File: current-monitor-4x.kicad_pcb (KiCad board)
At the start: 2 copper layers, 35 x 30 mm, 32 parts, among them J1 CONN-2, J2 CONN-2, J3 USB-MICROB, J4 JTAG, U1 ACS711EX, U2 ACS711EX, U3 MKL26ZxxVFM4, Y1 12MHz

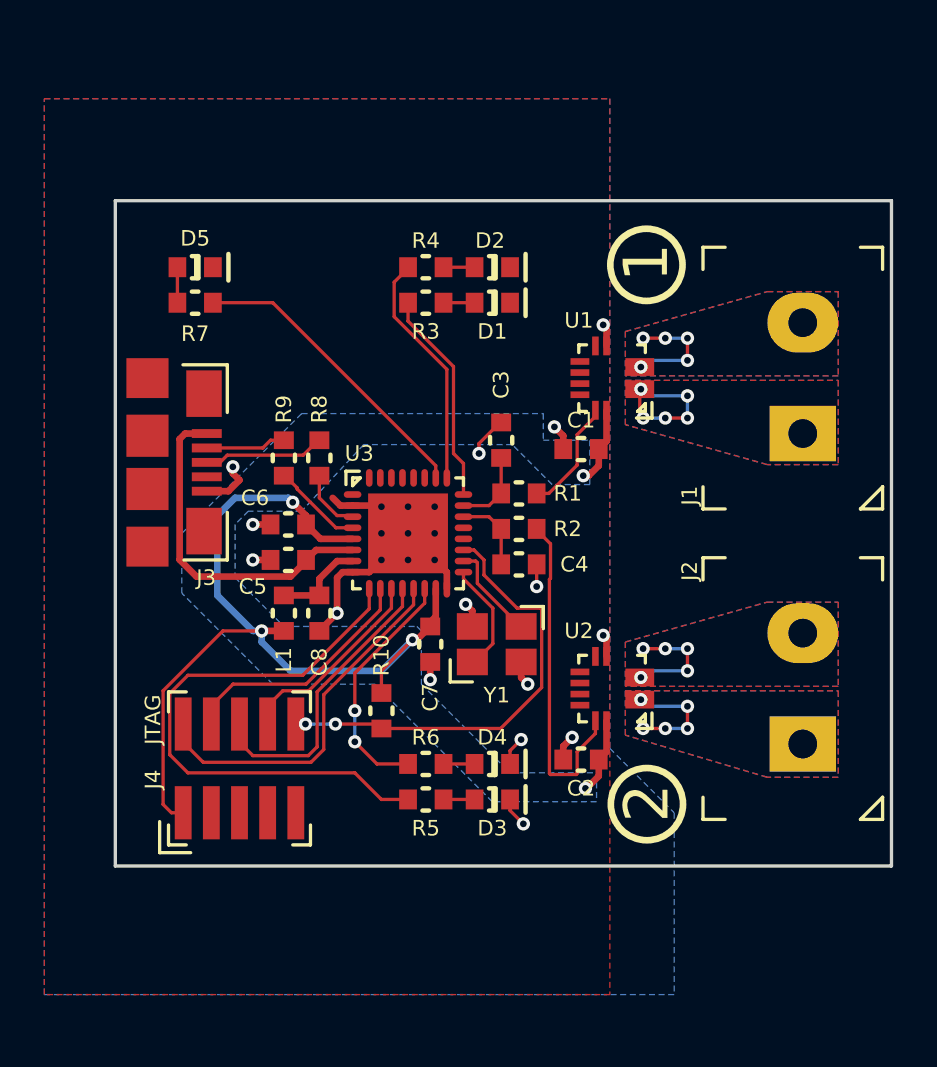
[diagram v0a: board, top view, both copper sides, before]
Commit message: add mounting lugs
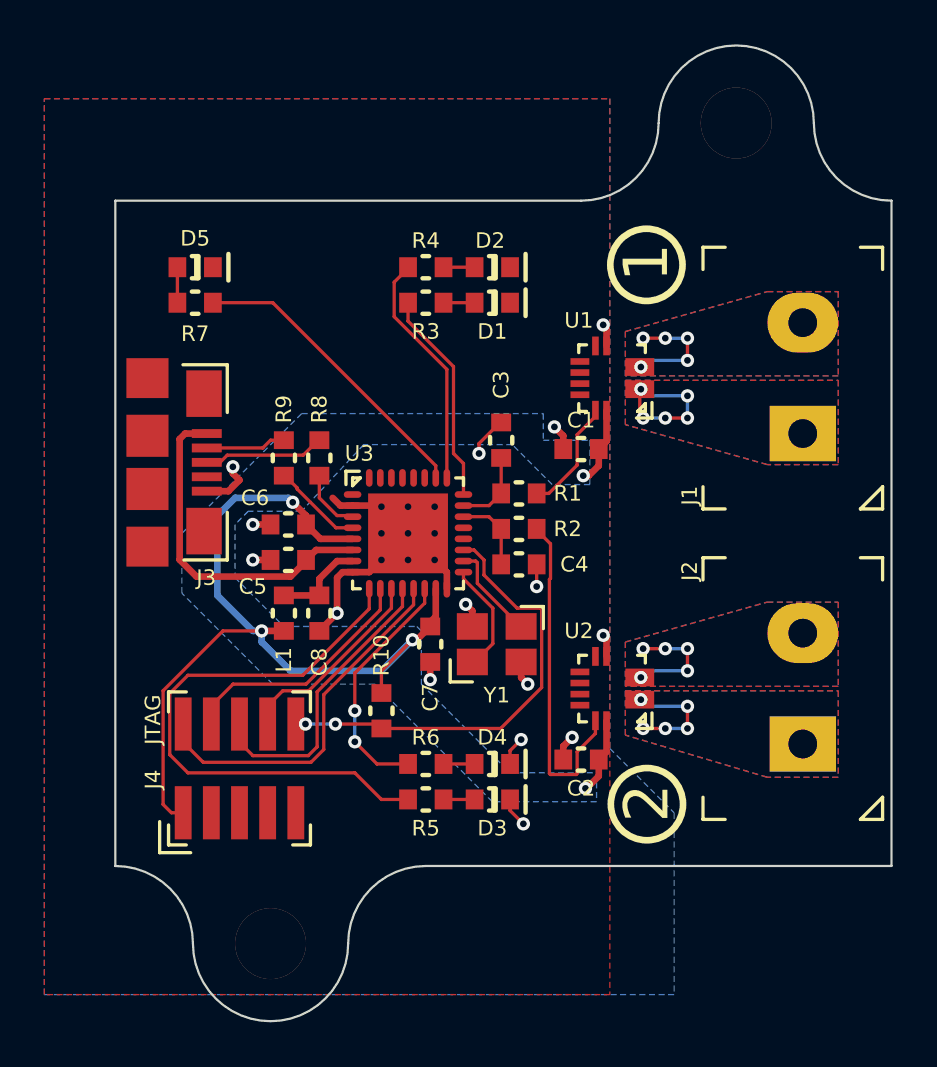
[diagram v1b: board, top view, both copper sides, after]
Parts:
- added REF**: M3-LUG, libs:M3-LUG, F.Cu at (170.0, 116.5)
- added REF**: M3-LUG, libs:M3-LUG, F.Cu at (191.0, 79.5)
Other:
- board size 35 x 30 mm -> 35 x 44 mm
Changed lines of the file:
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@@
     (links 97)
     (no_connects 0)
-    (area 162.924999 82.924999 198.075001 113.075001)
+    (area 162.949999 75.949999 198.050001 120.050001)
     (thickness 1.6)
-    (drawings 8)
+    (drawings 14)
     (tracks 282)
     (zones 0)
-    (modules 32)
+    (modules 34)
     (nets 34)
   )
   (page A4)
+  (title_block
+    (title "2x Isolated Current Monitor")
+    (date 2015-11-08)
+    (rev 1.0)
+    (company sternlabs)
+    (comment 1 "(c) 2015 Simon Schubert")
+  )
   (layers
     (0 F.Cu signal)
@@
     (trace_min 0.15)
     (segment_width 0.2)
-    (edge_width 0.15)
+    (edge_width 0.1)
     (via_size 0.6)
     (via_drill 0.3)
@@
     (add_net "Net-(U3-Pad17)")
     (add_net "Net-(U3-Pad18)")
+  )
+  (module libs:M3-LUG (layer F.Cu)
+    (at 170 116.5 180)
+    (fp_text reference REF** (at 0 0.5 180) (layer F.SilkS) hide
+      (effects (font (size 1 1) (thickness 0.15)))
+    )
+    (fp_text value M3-LUG (at 0 -0.5 180) (layer F.Fab) hide
+      (effects (font (size 1 1) (thickness 0.15)))
+    )
+    (fp_arc (start -7 0) (end -3.5 0) (angle 90) (layer Dwgs.User) (width 0.1))
+    (fp_arc (start 7 0) (end 3.5 0) (angle -90) (layer Dwgs.User) (width 0.1))
+    (fp_arc (start 0 0) (end -3.5 0) (angle 180) (layer Dwgs.User) (width 0.1))
+    (pad 1 thru_hole circle (at 0 0 180) (size 3.2 3.2) (drill 3.2) (layers *.Cu *.Mask))
   )
   (module libs:CONN-2x5-1.27-SMT (layer F.Cu)
@@
       (net 15 "Net-(J1-Pad2)") (thermal_width 0.5) (thermal_gap 0.3))
   )
+  (module libs:M3-LUG (layer F.Cu)
+    (at 191 79.5)
+    (fp_text reference REF** (at 0 0.5) (layer F.SilkS) hide
+      (effects (font (size 1 1) (thickness 0.15)))
+    )
+    (fp_text value M3-LUG (at 0 -0.5) (layer F.Fab) hide
+      (effects (font (size 1 1) (thickness 0.15)))
+    )
+    (fp_arc (start -7 0) (end -3.5 0) (angle 90) (layer Dwgs.User) (width 0.1))
+    (fp_arc (start 7 0) (end 3.5 0) (angle -90) (layer Dwgs.User) (width 0.1))
+    (fp_arc (start 0 0) (end -3.5 0) (angle 180) (layer Dwgs.User) (width 0.1))
+    (pad 1 thru_hole circle (at 0 0) (size 3.2 3.2) (drill 3.2) (layers *.Cu *.Mask))
+  )
+  (gr_arc (start 170 116.5) (end 173.5 116.5) (angle 180) (layer Edge.Cuts) (width 0.1))
+  (gr_arc (start 177 116.5) (end 173.5 116.5) (angle 90) (layer Edge.Cuts) (width 0.1))
+  (gr_arc (start 163 116.5) (end 163 113) (angle 90) (layer Edge.Cuts) (width 0.1))
+  (gr_line (start 198 113) (end 177 113) (layer Edge.Cuts) (width 0.1))
+  (gr_arc (start 191 79.5) (end 187.5 79.5) (angle 180) (layer Edge.Cuts) (width 0.1))
+  (gr_arc (start 198 79.5) (end 198 83) (angle 90) (layer Edge.Cuts) (width 0.1))
+  (gr_arc (start 184 79.5) (end 187.5 79.5) (angle 90) (layer Edge.Cuts) (width 0.1))
   (gr_text 2 (at 186.972507 110.162173 90) (layer F.SilkS)
     (effects (font (size 2 2) (thickness 0.3)))
@@
     (effects (font (size 2 2) (thickness 0.3)))
   )
-  (gr_line (start 163 83) (end 198 83) (layer Edge.Cuts) (width 0.15))
-  (gr_line (start 163 113) (end 163 83) (layer Edge.Cuts) (width 0.15))
-  (gr_line (start 198 113) (end 163 113) (layer Edge.Cuts) (width 0.15))
-  (gr_line (start 198 83) (end 198 113) (layer Edge.Cuts) (width 0.15))
+  (gr_line (start 163 83) (end 184 83) (layer Edge.Cuts) (width 0.1))
+  (gr_line (start 163 113) (end 163 83) (layer Edge.Cuts) (width 0.1))
+  (gr_line (start 198 83) (end 198 113) (layer Edge.Cuts) (width 0.1))
   (segment (start 184.35 95.4) (end 184.1 95.4) (width 0.3) (layer F.Cu) (net 1))
   (segment (start 184.8 94.95) (end 184.35 95.4) (width 0.3) (layer F.Cu) (net 1))

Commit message: fix zone layout
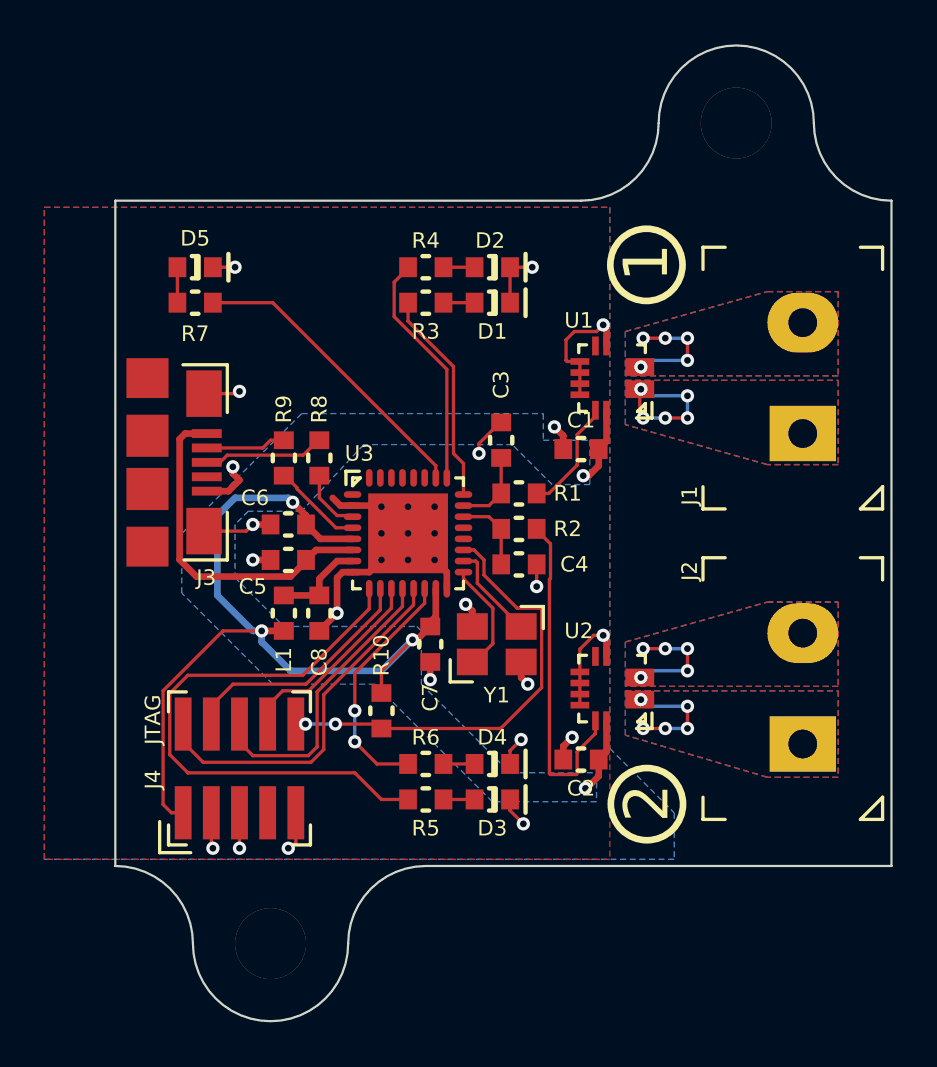
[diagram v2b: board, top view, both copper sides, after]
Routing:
- net COM: track 25.9 -> 47.3 mm, vias 15 -> 21
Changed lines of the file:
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@@
     (thickness 1.6)
     (drawings 14)
-    (tracks 282)
+    (tracks 317)
     (zones 0)
     (modules 34)
@@
   (title_block
     (title "2x Isolated Current Monitor")
-    (date 2015-11-08)
+    (date 2015-11-09)
     (rev 1.0)
     (company sternlabs)
@@
     (add_net "Net-(U3-Pad17)")
     (add_net "Net-(U3-Pad18)")
-  )
-  (module libs:M3-LUG (layer F.Cu)
-    (at 170 116.5 180)
-    (fp_text reference REF** (at 0 0.5 180) (layer F.SilkS) hide
-      (effects (font (size 1 1) (thickness 0.15)))
-    )
-    (fp_text value M3-LUG (at 0 -0.5 180) (layer F.Fab) hide
-      (effects (font (size 1 1) (thickness 0.15)))
-    )
-    (fp_arc (start -7 0) (end -3.5 0) (angle 90) (layer Dwgs.User) (width 0.1))
-    (fp_arc (start 7 0) (end 3.5 0) (angle -90) (layer Dwgs.User) (width 0.1))
-    (fp_arc (start 0 0) (end -3.5 0) (angle 180) (layer Dwgs.User) (width 0.1))
-    (pad 1 thru_hole circle (at 0 0 180) (size 3.2 3.2) (drill 3.2) (layers *.Cu *.Mask))
   )
   (module libs:CONN-2x5-1.27-SMT (layer F.Cu)
@@
       (effects (font (size 1 1) (thickness 0.15)))
     )
+    (fp_line (start 7 3.5) (end -7 3.5) (layer Margin) (width 0.1))
     (fp_arc (start -7 0) (end -3.5 0) (angle 90) (layer Dwgs.User) (width 0.1))
     (fp_arc (start 7 0) (end 3.5 0) (angle -90) (layer Dwgs.User) (width 0.1))
     (fp_arc (start 0 0) (end -3.5 0) (angle 180) (layer Dwgs.User) (width 0.1))
     (pad 1 thru_hole circle (at 0 0) (size 3.2 3.2) (drill 3.2) (layers *.Cu *.Mask))
+  )
+  (module libs:M3-LUG (layer F.Cu)
+    (at 170 116.5 180)
+    (fp_text reference REF** (at 0 0.5 180) (layer F.SilkS) hide
+      (effects (font (size 1 1) (thickness 0.15)))
+    )
+    (fp_text value M3-LUG (at 0 -0.5 180) (layer F.Fab) hide
+      (effects (font (size 1 1) (thickness 0.15)))
+    )
+    (fp_line (start 7 3.5) (end -7 3.5) (layer Margin) (width 0.1))
+    (fp_arc (start -7 0) (end -3.5 0) (angle 90) (layer Dwgs.User) (width 0.1))
+    (fp_arc (start 7 0) (end 3.5 0) (angle -90) (layer Dwgs.User) (width 0.1))
+    (fp_arc (start 0 0) (end -3.5 0) (angle 180) (layer Dwgs.User) (width 0.1))
+    (pad 1 thru_hole circle (at 0 0 180) (size 3.2 3.2) (drill 3.2) (layers *.Cu *.Mask))
   )
   (gr_arc (start 170 116.5) (end 173.5 116.5) (angle 180) (layer Edge.Cuts) (width 0.1))
@@
   (segment (start 173.7 98.25) (end 172.25 98.25) (width 0.3) (layer F.Cu) (net 1) (status 10))
   (segment (start 172.25 98.25) (end 171.6 97.6) (width 0.3) (layer F.Cu) (net 1) (status 20))
+  (segment (start 183.95 104.25) (end 183.95 103.225744) (width 0.15) (layer F.Cu) (net 2))
+  (segment (start 183.95 103.225744) (end 184.575736 102.600008) (width 0.15) (layer F.Cu) (net 2))
+  (segment (start 184.575736 102.600008) (end 185 102.600008) (width 0.15) (layer F.Cu) (net 2))
+  (segment (start 183.95 104.75) (end 183.95 104.25) (width 0.15) (layer F.Cu) (net 2))
+  (segment (start 183.95 105.25) (end 183.95 104.75) (width 0.15) (layer F.Cu) (net 2))
+  (segment (start 183.95 105.75) (end 183.95 105.25) (width 0.15) (layer F.Cu) (net 2))
+  (segment (start 167.4 86) (end 168.4 86) (width 0.15) (layer F.Cu) (net 2))
+  (via (at 168.4 86) (size 0.6) (drill 0.3) (layers F.Cu B.Cu) (net 2))
+  (segment (start 167 91.7) (end 168.5 91.7) (width 0.15) (layer F.Cu) (net 2))
+  (segment (start 168.5 91.7) (end 168.6 91.6) (width 0.15) (layer F.Cu) (net 2))
+  (via (at 168.6 91.6) (size 0.6) (drill 0.3) (layers F.Cu B.Cu) (net 2))
+  (segment (start 167 97.9) (end 168.900001 97.899999) (width 0.15) (layer F.Cu) (net 2))
+  (segment (start 168.900001 97.899999) (end 169.2 97.6) (width 0.15) (layer F.Cu) (net 2))
+  (segment (start 171.14 110.6) (end 171.14 111.95) (width 0.15) (layer F.Cu) (net 2))
+  (segment (start 171.14 111.95) (end 170.89 112.2) (width 0.15) (layer F.Cu) (net 2))
+  (segment (start 170.89 112.2) (end 170.8 112.2) (width 0.15) (layer F.Cu) (net 2))
+  (via (at 170.8 112.2) (size 0.6) (drill 0.3) (layers F.Cu B.Cu) (net 2))
+  (segment (start 168.6 110.6) (end 168.6 111.95) (width 0.15) (layer F.Cu) (net 2))
+  (segment (start 168.6 111.95) (end 168.6 112.2) (width 0.15) (layer F.Cu) (net 2))
+  (via (at 168.6 112.2) (size 0.6) (drill 0.3) (layers F.Cu B.Cu) (net 2))
+  (segment (start 167.33 110.6) (end 167.33 112.13) (width 0.15) (layer F.Cu) (net 2))
+  (segment (start 167.33 112.13) (end 167.4 112.2) (width 0.15) (layer F.Cu) (net 2))
+  (via (at 167.4 112.2) (size 0.6) (drill 0.3) (layers F.Cu B.Cu) (net 2))
+  (segment (start 183.325 89.275) (end 183.700001 88.899999) (width 0.15) (layer F.Cu) (net 2))
+  (segment (start 183.700001 88.899999) (end 184.700011 88.899999) (width 0.15) (layer F.Cu) (net 2))
+  (segment (start 184.700011 88.899999) (end 185.00001 88.6) (width 0.15) (layer F.Cu) (net 2))
+  (segment (start 183.325 90.2) (end 183.325 89.275) (width 0.15) (layer F.Cu) (net 2))
+  (segment (start 183.95 90.25) (end 183.375 90.25) (width 0.15) (layer F.Cu) (net 2))
+  (segment (start 183.375 90.25) (end 183.325 90.2) (width 0.15) (layer F.Cu) (net 2))
+  (segment (start 183.95 90.75) (end 183.95 90.25) (width 0.15) (layer F.Cu) (net 2))
+  (segment (start 183.95 91.25) (end 183.95 90.75) (width 0.15) (layer F.Cu) (net 2))
+  (segment (start 183.95 91.75) (end 183.95 91.25) (width 0.15) (layer F.Cu) (net 2))
+  (segment (start 180.8 86) (end 181.8 86) (width 0.15) (layer F.Cu) (net 2))
+  (via (at 181.8 86) (size 0.6) (drill 0.3) (layers F.Cu B.Cu) (net 2))
+  (segment (start 180.8 87.6) (end 180.8 86) (width 0.15) (layer F.Cu) (net 2))
   (segment (start 180.8 110) (end 180.8 110.5) (width 0.15) (layer F.Cu) (net 2))
   (segment (start 180.8 110.5) (end 181.4 111.1) (width 0.15) (layer F.Cu) (net 2))
@@
     (polygon
       (pts
-        (xy 159.8 118.8) (xy 159.8 78.4) (xy 185.3 78.4) (xy 185.3 118.8)
+        (xy 159.8 112.7) (xy 159.8 83.3) (xy 185.3 83.3) (xy 185.3 112.7)
       )
     )
@@
     (polygon
       (pts
-        (xy 159.8 118.8) (xy 159.8 78.4) (xy 185.3 78.4) (xy 185.3 107.7) (xy 188.2 110.6)
-        (xy 188.2 118.8)
+        (xy 159.8 112.7) (xy 159.8 83.3) (xy 185.3 83.3) (xy 185.3 107.7) (xy 188.2 110.6)
+        (xy 188.2 112.7)
       )
     )
